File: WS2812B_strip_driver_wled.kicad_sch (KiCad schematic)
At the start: 114 parts, among them J1 CH_1, J2 CH_2, J3 CH_3, J4 CH_4, J5 PWR_IN, J6 uPhone, J8 USB_C_Receptacle_USB2.0_16P, K1 RELAY_1, K2 RELAY_2, K3 RELAY_3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

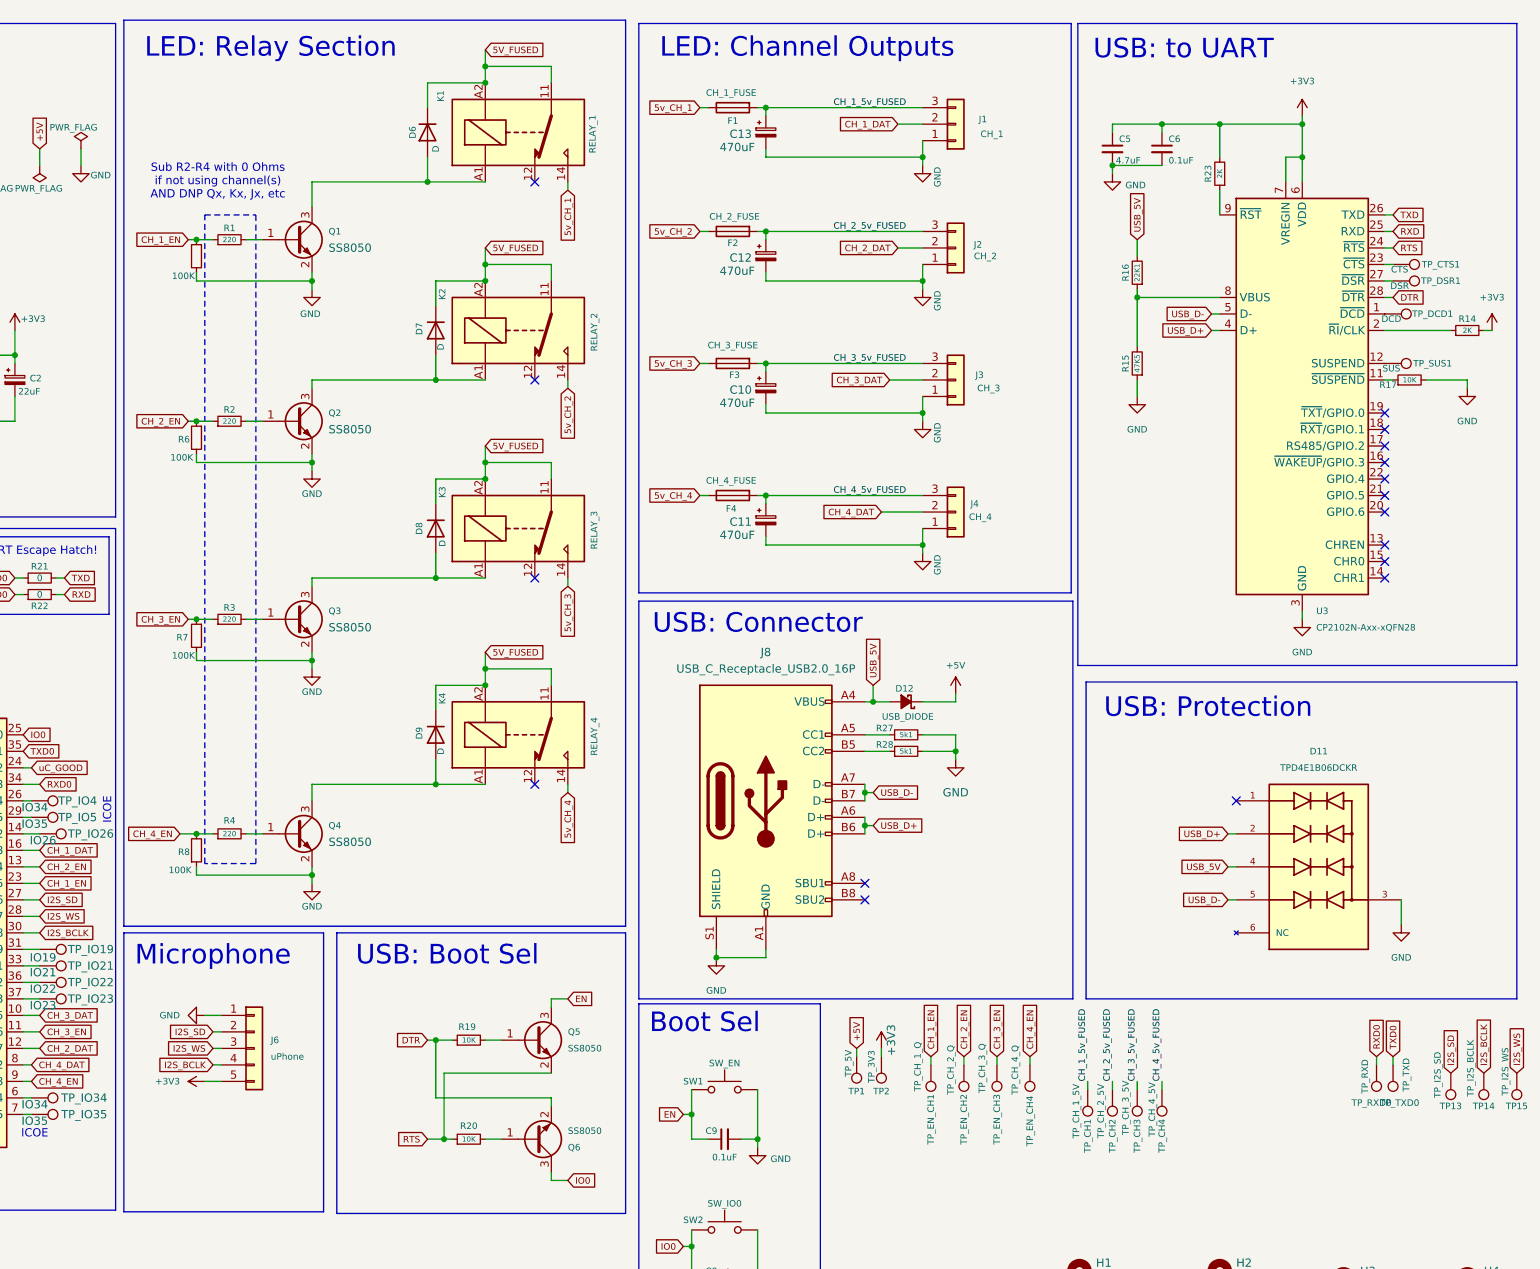
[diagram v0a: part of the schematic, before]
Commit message: added 0402 zero-ohm for solder-blob jumpering the channels. Even better silkscreen
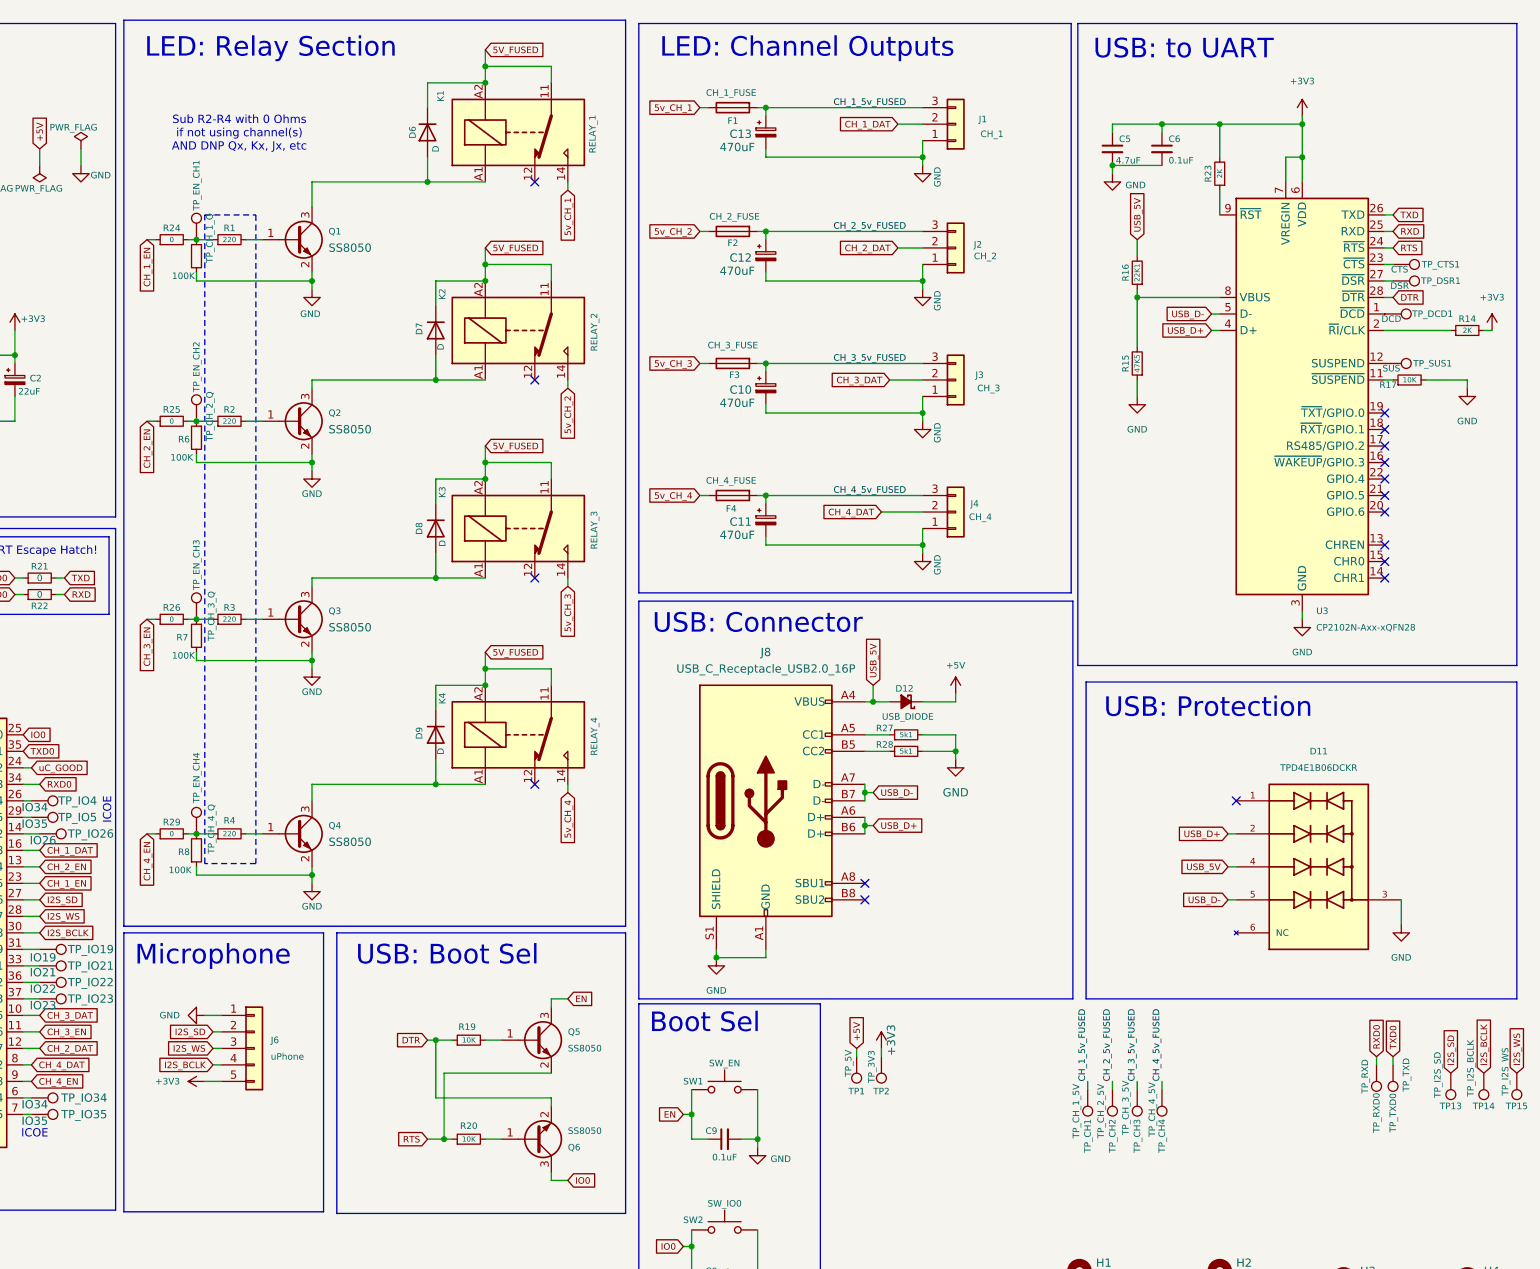
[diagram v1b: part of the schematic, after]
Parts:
- added R24, R25, R26, R29: 0, Resistor_SMD:R_0402_1005Metric, symbol Device:R_Small
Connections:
- net CH_1_EN: now also R24.1; no longer R1.1, R5.1, TP_EN_CH1.1
- net CH_2_EN: now also R25.1; no longer R2.1, R6.1, TP_EN_CH2.1
- net CH_3_EN: now also R26.1; no longer R3.1, R7.1, TP_EN_CH3.1
- net CH_4_EN: now also R29.1; no longer R4.1, R8.2, TP_EN_CH4.1
- new net: R29.2, R4.1, R8.2, TP_EN_CH4.1
- new net: R2.1, R25.2, R6.1, TP_EN_CH2.1
- new net: R1.1, R24.2, R5.1, TP_EN_CH1.1
- new net: R26.2, R3.1, R7.1, TP_EN_CH3.1
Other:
- moved on the sheet: TP_EN_CH1, TP_EN_CH2, TP_EN_CH3, TP_EN_CH4

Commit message: cleaned up schematic. assigned esp32e as my custom version with 0.3mm vias to stop drc warnings
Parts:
- J1, J2, J3, J4: symbol Connector_Generic:Conn_01x03 -> Connector:Screw_Terminal_01x03
- R41: value 170 -> 170R
- U1: footprint RF_Module:ESP32-WROOM-32E -> JIMS_MCUS:ESP32-WROOM-32E-0.3VIAS
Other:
- note added: "Connector"
- note added: "Make ERC Happy!"
- note added: "Protection"
- note added: "USB"
- note added: "Uart Testpoints"
- note removed: "TODO: DONE - ADD TVS DIODES TO USB DONE - ADD BTNS TO SCHEMATIC (RSt/BOOT) DONE - ADD CAPS TO O/PUTS? ADD CAPS TO USB MPs? DONE - ADD TP's DONE - FIND OUT current CH_1-3 relay and data lines DONE - FIND OUT current uPhone Data Lines DONE - FIND TWO NEW O/PUTS for RELAY4 and DAT4 DECIDE ON OFFBOARD CONNECTORS"
- note removed: "USB: Connector"
- note removed: "USB: Protection"
- moved on the sheet: C1, C2, C5, C6, C8, C9, D11, D12, F5, H1, H2, H3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

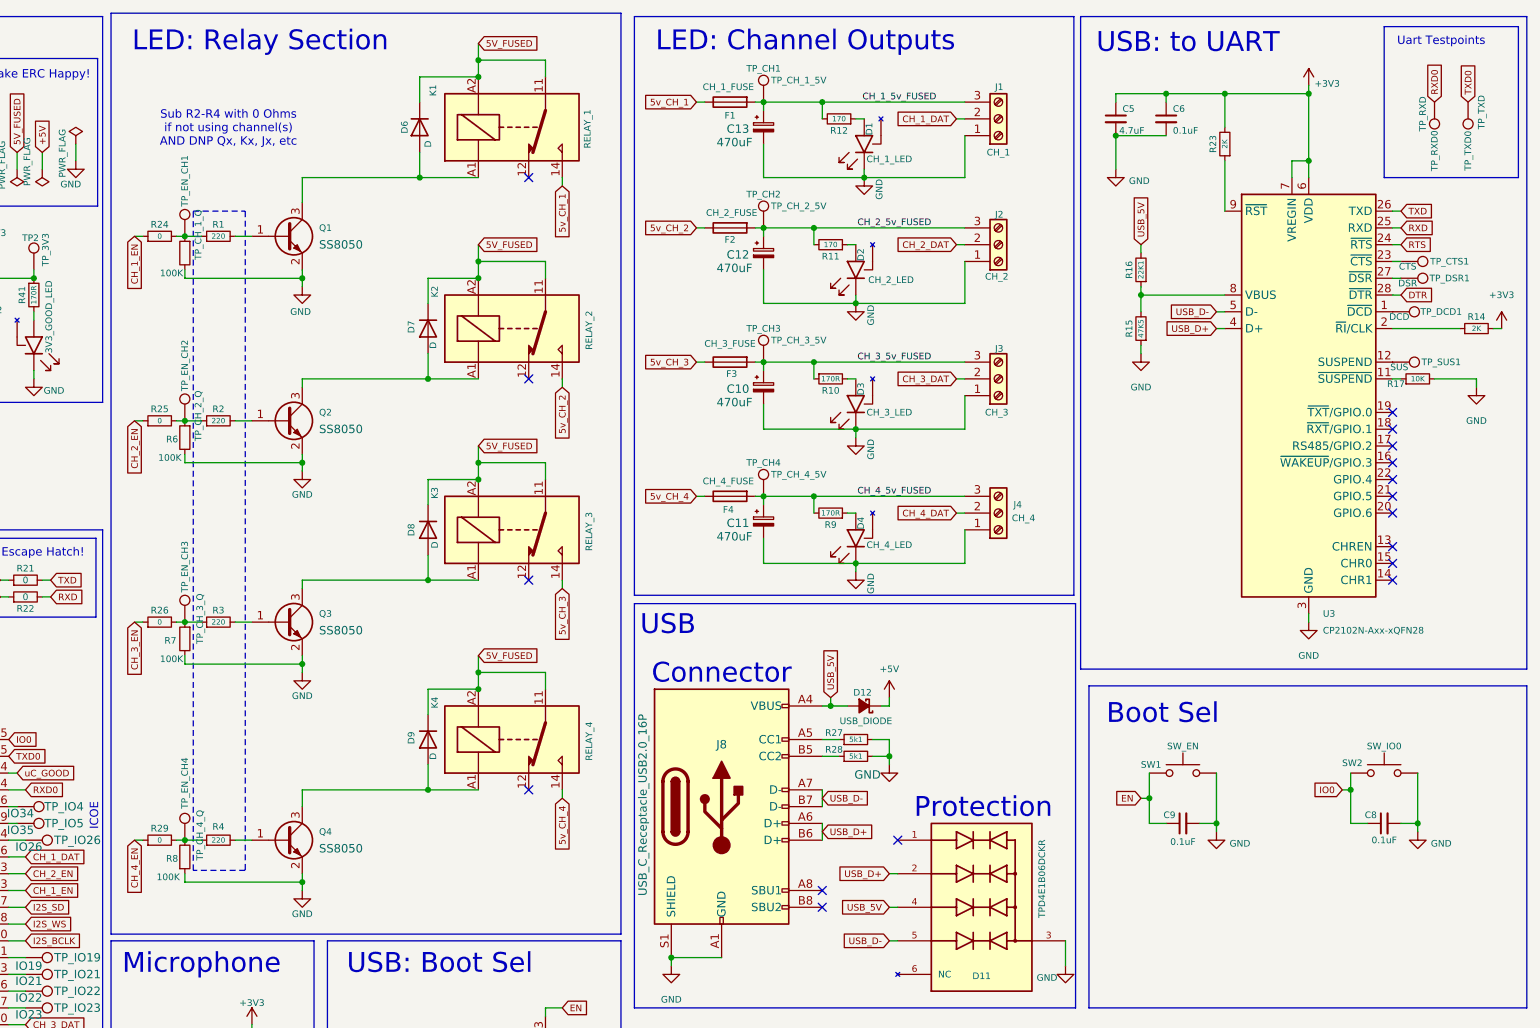
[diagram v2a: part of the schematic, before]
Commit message: updated readme with licence info, brief description and some images
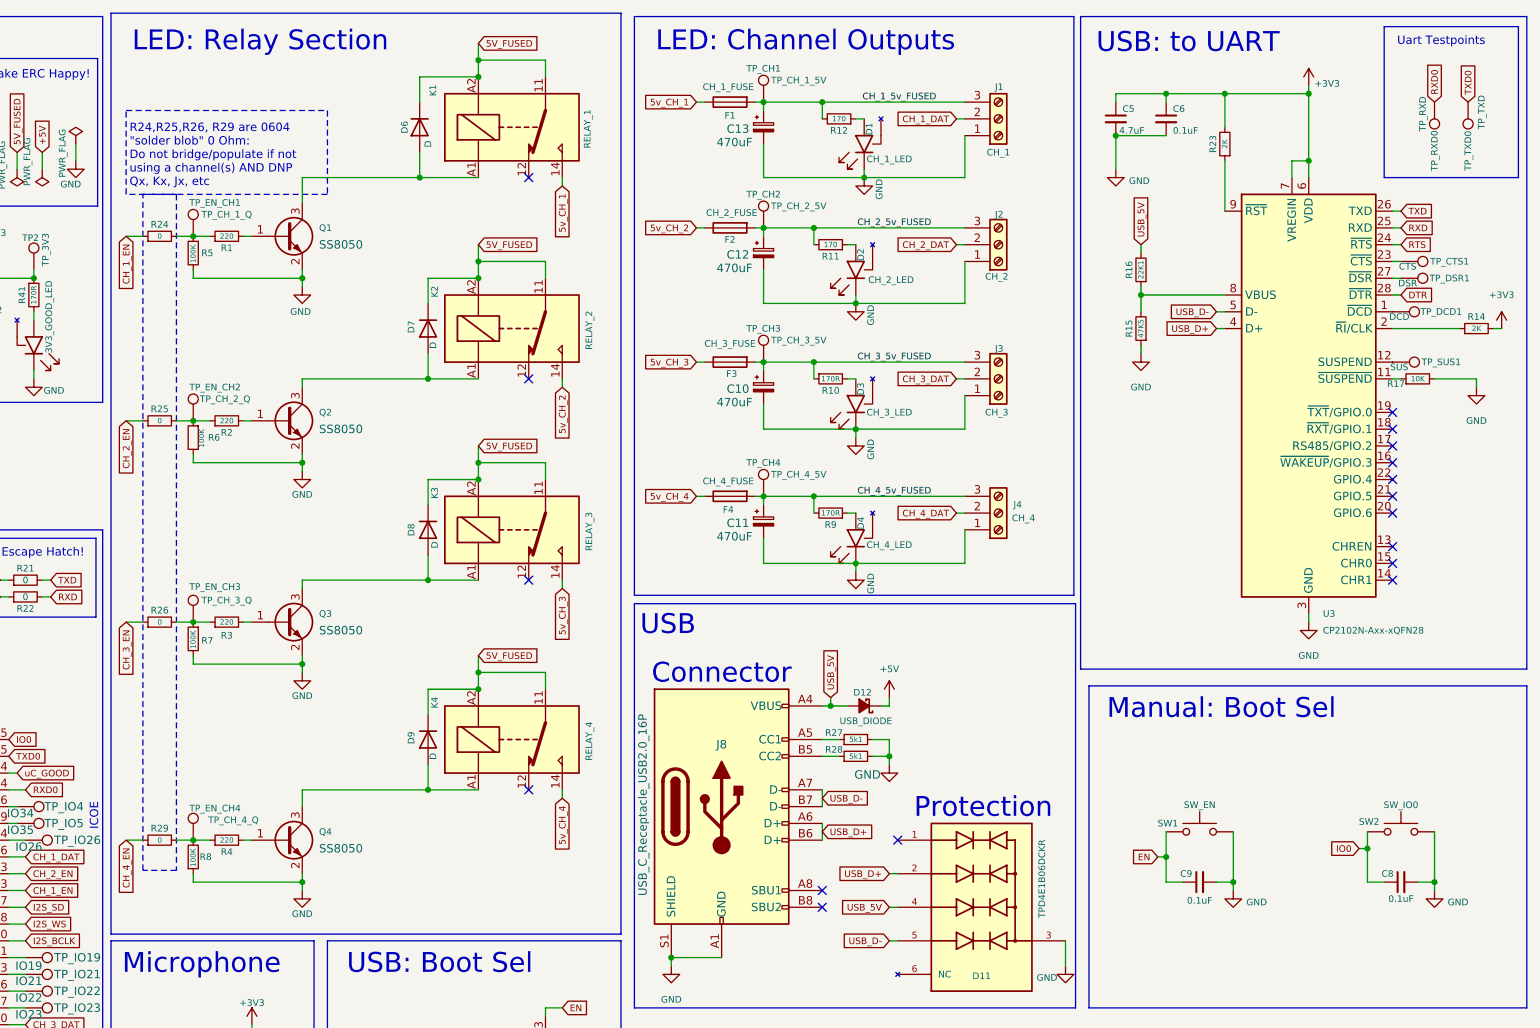
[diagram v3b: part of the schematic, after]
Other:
- note added: "Manual: Boot Sel"
- note added: "R24,R25,R26, R29 are 0604 "solder blob" 0 Ohm: Do not bridge/populate if not using a channel(s) AND DNP Qx, Kx, Jx, etc"
- note removed: "Boot Sel"
- note removed: "Sub R2-R4 with 0 Ohms if not using channel(s) AND DNP Qx, Kx, Jx, etc"
- moved on the sheet: C8, C9, R1, R2, R3, R4, R6, R7, R8, SW1, SW2, TP_EN_CH1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
